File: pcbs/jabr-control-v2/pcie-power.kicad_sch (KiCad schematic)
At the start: 29 parts, among them U1501 TPS22991CNRAAR, U1502 TPS62824DMQR, U1503 TPS62824DMQR

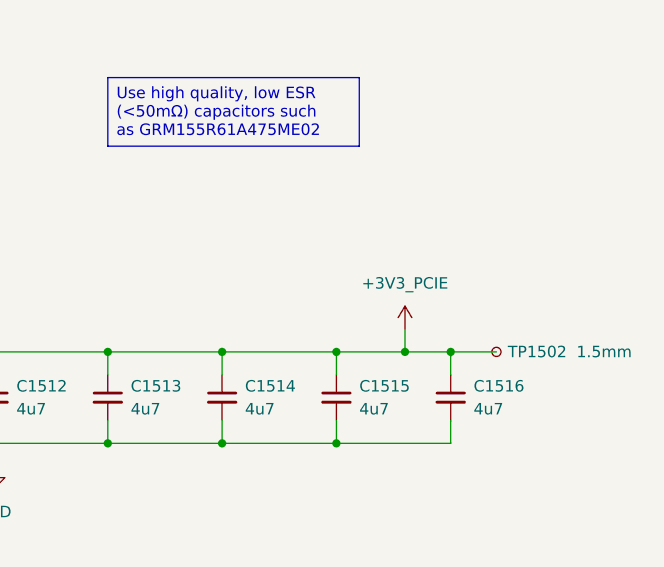
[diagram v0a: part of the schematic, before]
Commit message: PCI11010 IO done
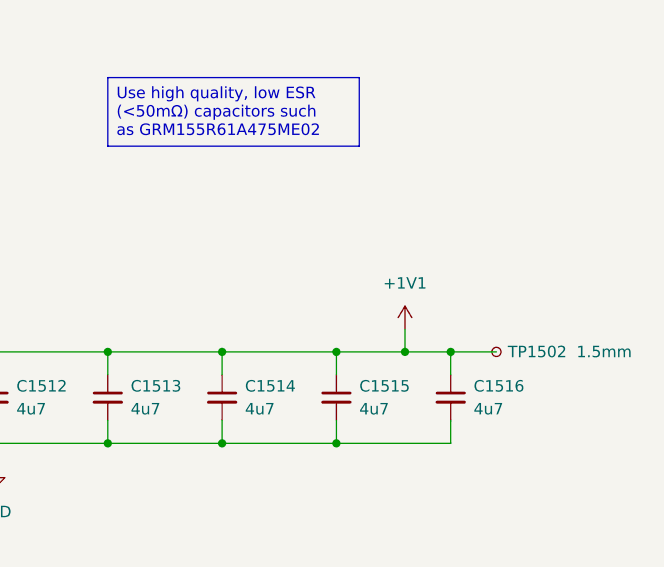
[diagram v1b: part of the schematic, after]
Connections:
- net +3V3_PCIE: no longer C1511.1, C1512.1, C1513.1, C1514.1, C1515.1, C1516.1, L1502.2, R1504.1, TP1502.1
- new net +1V1: C1511.1, C1512.1, C1513.1, C1514.1, C1515.1, C1516.1, L1502.2, R1504.1, TP1502.1
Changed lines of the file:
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@@
+	)
+	(symbol
+		(lib_id "power:+1V1")
+		(at 228.6 139.7 0)
+		(unit 1)
+		(body_style 1)
+		(exclude_from_sim no)
+		(in_bom yes)
+		(on_board yes)
+		(in_pos_files yes)
+		(dnp no)
+		(fields_autoplaced yes)
+		(property "Reference" "#PWR01508"
+			(at 228.6 143.51 0)
+			(hide yes)
+			(show_name no)
+			(do_not_autoplace no)
+			(effects
+				(font
+					(size 1.27 1.27)
+				)
+			)
+		)
+		(property "Value" "+1V1"
+			(at 228.6 134.62 0)
+			(show_name no)
+			(do_not_autoplace no)
+			(effects
+				(font
+					(size 1.27 1.27)
+				)
+			)
+		)
+		(property "Footprint" ""
+			(at 228.6 139.7 0)
+			(hide yes)
+			(show_name no)
+			(do_not_autoplace no)
+			(effects
+				(font
+					(size 1.27 1.27)
+				)
+			)
+		)
+		(property "Datasheet" ""
+			(at 228.6 139.7 0)
+			(hide yes)
+			(show_name no)
+			(do_not_autoplace no)
+			(effects
+				(font
+					(size 1.27 1.27)
+				)
+			)
+		)
+		(property "Description" "Power symbol creates a global label with name \"+1V1\""
+			(at 228.6 139.7 0)
+			(hide yes)
+			(show_name no)
+			(do_not_autoplace no)
+			(effects
+				(font
+					(size 1.27 1.27)
+				)
+			)
+		)
+		(pin "1"
+		)
+		(instances
+			(project "jabr-control-v2"
+				(path "/f91ec272-d09a-4038-bbbb-962739a92c51/3f551047-3bb0-4f63-99e0-34fd9061d844/313ad2b1-6281-4d61-a8a6-55e55641e36c"
+					(reference "#PWR01508")
+					(unit 1)
+				)
+			)
+		)
 	)
 	(symbol
@@
 					(unit 1)
 				)
-			)
-		)
-	)
-	(symbol
-		(lib_id "PWR-SYM:+3V3_PCIE")
-		(at 228.6 139.7 0)
-		(unit 1)
-		(body_style 1)
-		(exclude_from_sim no)
-		(in_bom yes)
-		(on_board yes)
-		(in_pos_files yes)
-		(dnp no)
-		(fields_autoplaced yes)
-		(property "Reference" "#PWR01519"
-			(at 228.6 143.51 0)
-			(hide yes)
-			(show_name no)
-			(do_not_autoplace no)
-			(effects
-				(font
-					(size 1.27 1.27)
-				)
-			)
-		)
-		(property "Value" "+3V3_PCIE"
-			(at 228.6 134.62 0)
-			(show_name no)
-			(do_not_autoplace no)
-			(effects
-				(font
-					(size 1.27 1.27)
-				)
-			)
-		)
-		(property "Footprint" ""
-			(at 228.6 139.7 0)
-			(hide yes)
-			(show_name no)
-			(do_not_autoplace no)
-			(effects
-				(font
-					(size 1.27 1.27)
-				)
-			)
-		)
-		(property "Datasheet" ""
-			(at 228.6 139.7 0)
-			(hide yes)
-			(show_name no)
-			(do_not_autoplace no)
-			(effects
-				(font
-					(size 1.27 1.27)
-				)
-			)
-		)
-		(property "Description" "Power symbol creates a global label with name \"+3V3_PCIE\""
-			(at 228.6 139.7 0)
-			(hide yes)
-			(show_name no)
-			(do_not_autoplace no)
-			(effects
-				(font
-					(size 1.27 1.27)
-				)
-			)
-		)
-		(pin "1"
-		)
-		(instances
-			(project "jabr-control-v2"
-				(path "/f91ec272-d09a-4038-bbbb-962739a92c51/3f551047-3bb0-4f63-99e0-34fd9061d844/313ad2b1-6281-4d61-a8a6-55e55641e36c"
-					(reference "#PWR01519")
-					(unit 1)
-				)

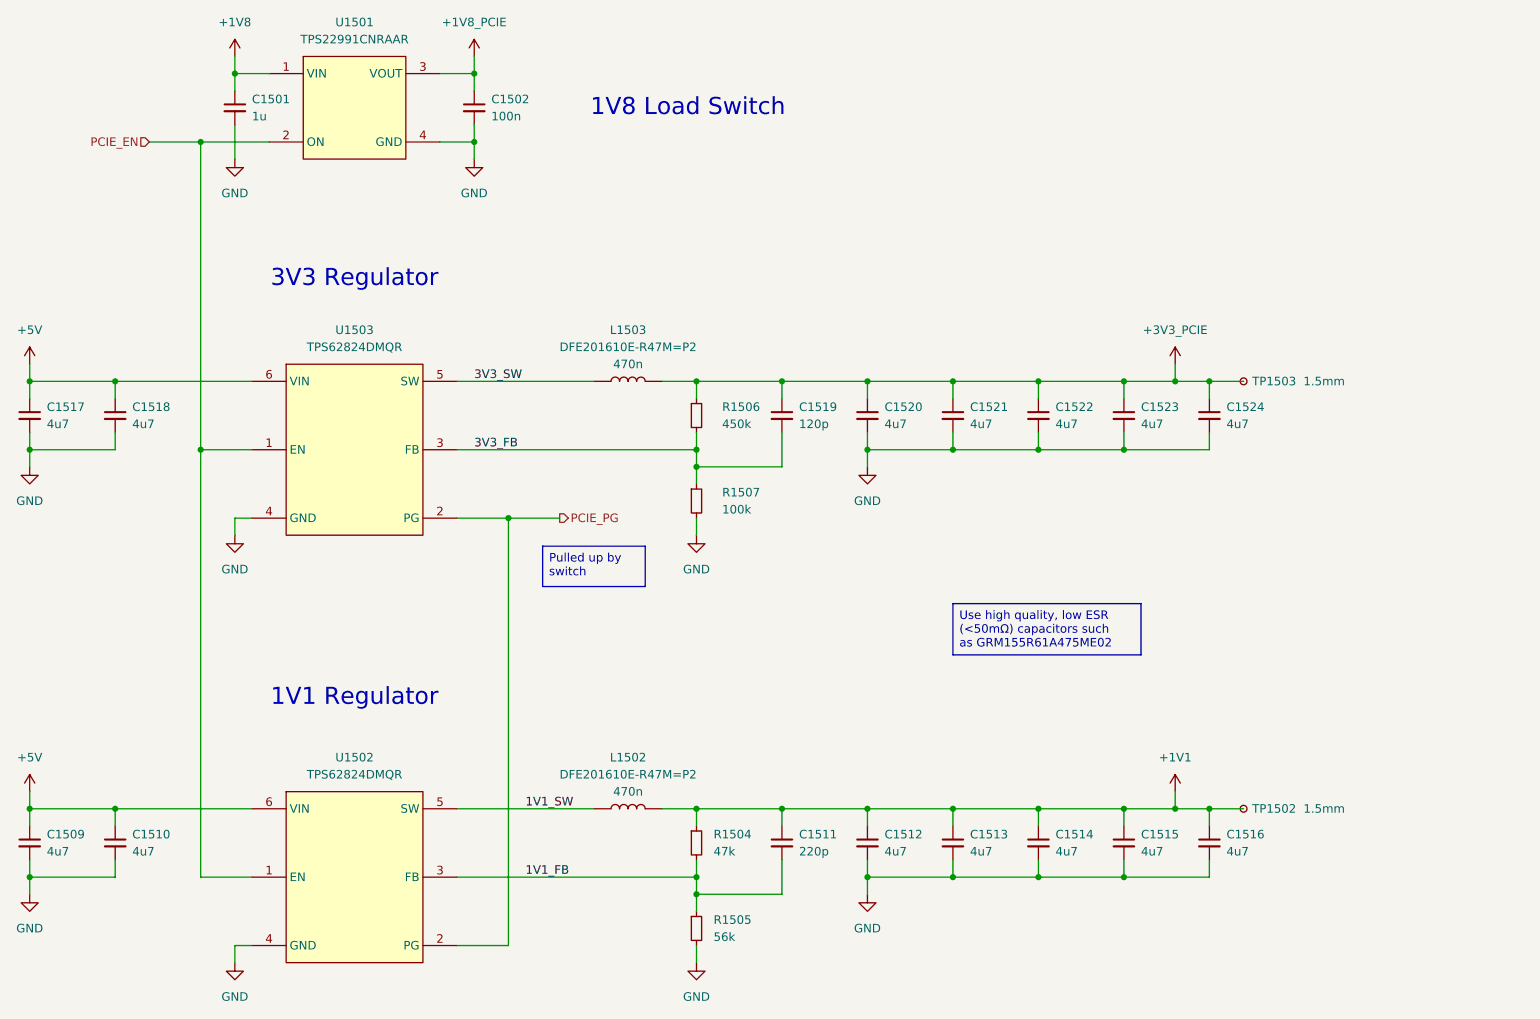
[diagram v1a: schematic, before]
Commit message: Removed power button reset to switch (power will be cycled anyway)
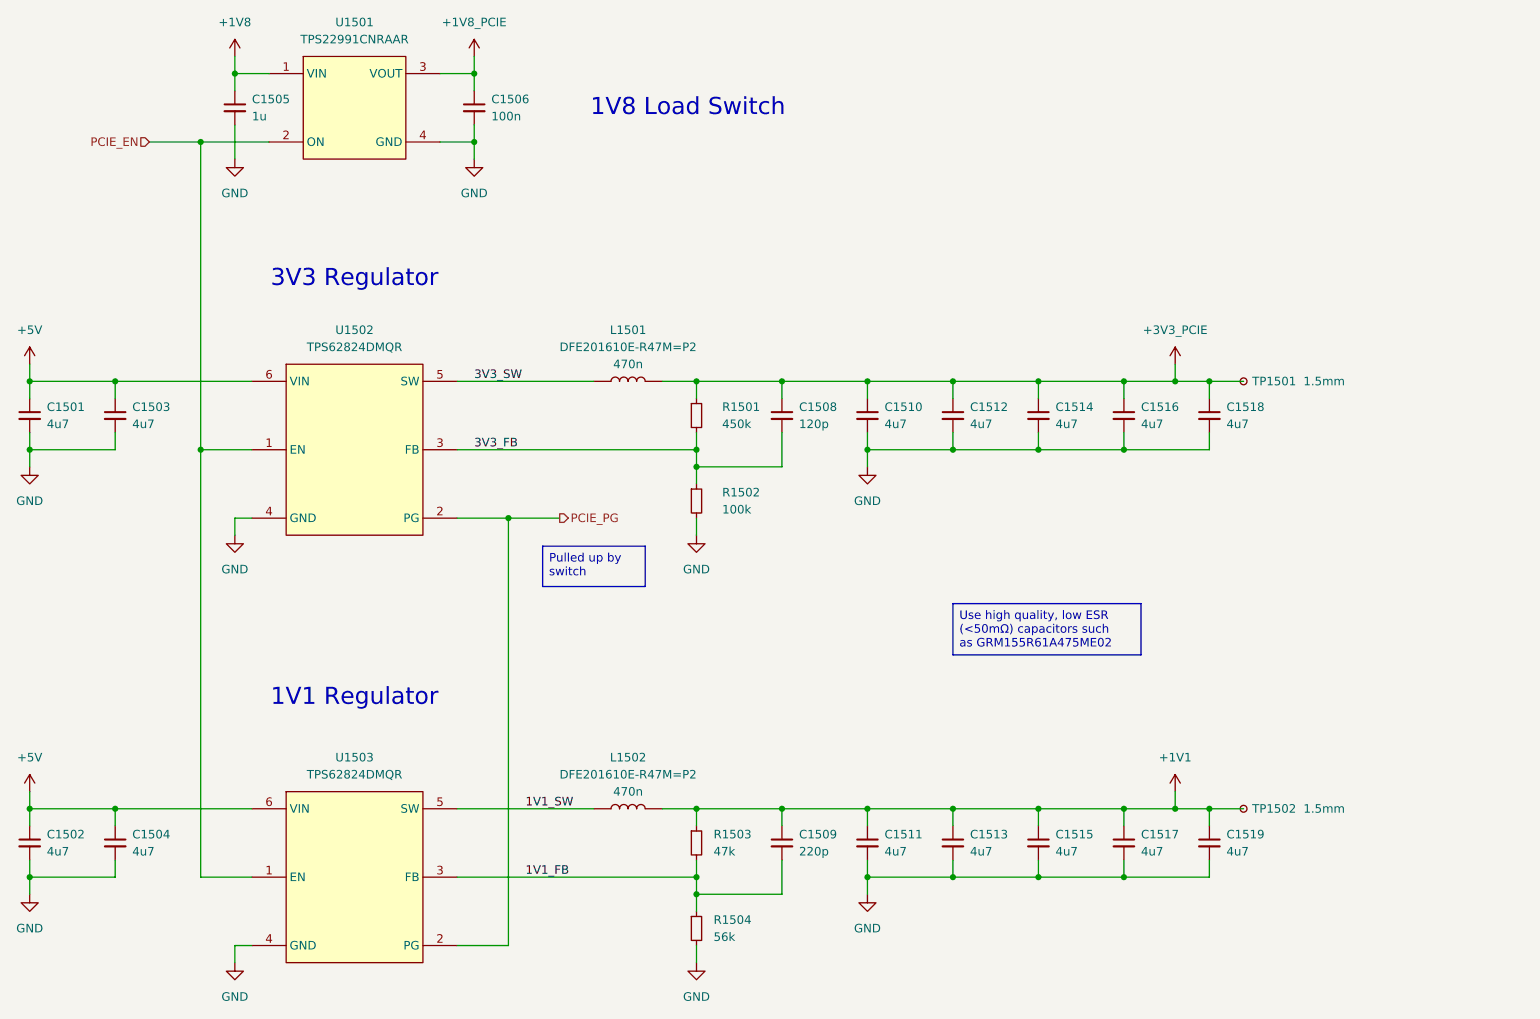
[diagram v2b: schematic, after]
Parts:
- renumbered C1517 to C1501, C1509 to C1502, C1518 to C1503, C1510 to C1504, C1501 to C1505, C1502 to C1506, C1519 to C1508, C1511 to C1509, C1520 to C1510, C1512 to C1511, C1521 to C1512, C1522 to C1514, C1514 to C1515, C1523 to C1516, C1515 to C1517, C1524 to C1518, C1516 to C1519, L1503 to L1501, R1506 to R1501, R1507 to R1502, R1504 to R1503, R1505 to R1504, TP1503 to TP1501, U1503 to U1502, U1502 to U1503

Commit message: Schematic done
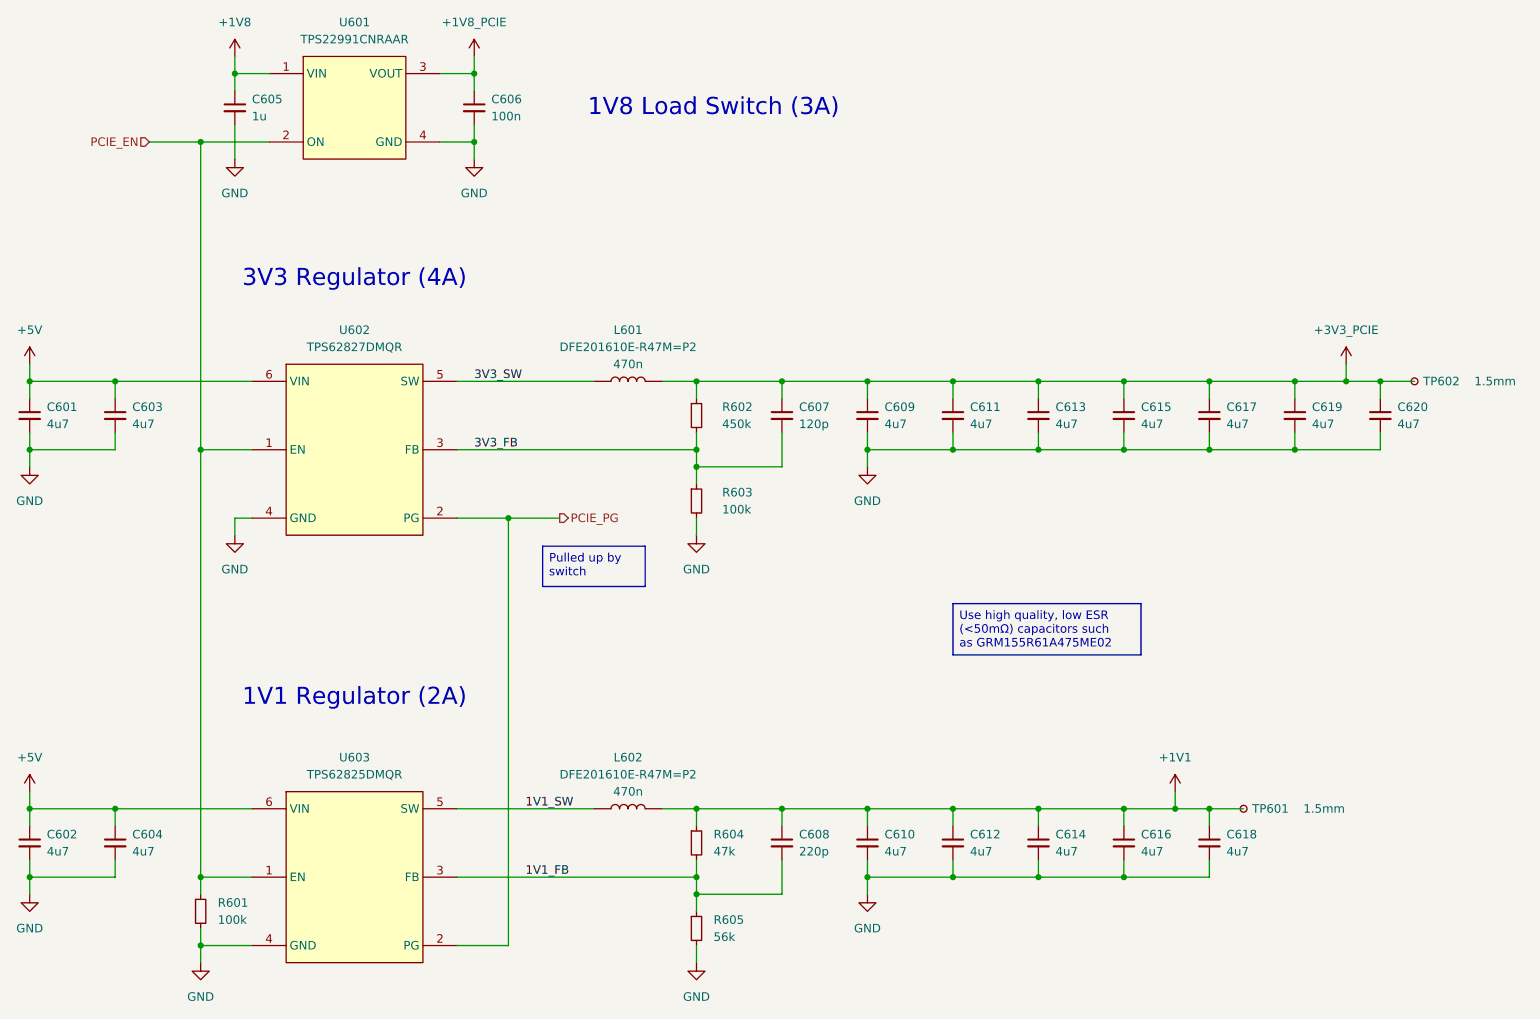
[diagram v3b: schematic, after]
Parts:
- removed U1502: TPS62824DMQR, project_footprints:TPS6282xDMQR, symbol PWR-SMPS:TPS62824DMQR
- added C615, C617: 4u7, project_footprints:C_0402, symbol DEV:C_SMALL
- added R601: 100k, project_footprints:R_0402, symbol Device:R_Small
- added U602: TPS62827DMQR, project_footprints:TPS6282xDMQR, symbol PWR-SMPS:TPS62827DMQR
- U603: renamed from U1503; value TPS62824DMQR -> TPS62825DMQR; symbol PWR-SMPS:TPS62824DMQR -> PWR-SMPS:TPS62825DMQR
- renumbered C1501 to C601, C1502 to C602, C1503 to C603, C1504 to C604, C1505 to C605, C1506 to C606, C1508 to C607, C1509 to C608, C1510 to C609, C1511 to C610, C1512 to C611, C1513 to C612, C1514 to C613, C1515 to C614, C1517 to C616, C1519 to C618, C1516 to C619, C1518 to C620, L1501 to L601, L1502 to L602, R1501 to R602, R1502 to R603, R1503 to R604, R1504 to R605, TP1502 to TP601, TP1501 to TP602, U1501 to U601
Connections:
- net +3V3_PCIE: now also C615.1, C617.1
- net +5V: now also U602.6 (VIN)
- net 3V3_FB: now also U602.3 (FB)
- net 3V3_SW: now also U602.5 (SW)
- net GND: now also C615.2, C617.2, R601.2, U602.4 (GND)
- net PCIE_EN: now also R601.1, U602.1 (EN)
- net PCIE_PG: now also U602.2 (PG)
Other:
- note added: "1V1 Regulator (2A)"
- note added: "1V8 Load Switch (3A)"
- note added: "3V3 Regulator (4A)"
- note removed: "1V1 Regulator"
- note removed: "1V8 Load Switch"
- note removed: "3V3 Regulator"
- moved on the sheet: C619, C620, TP602
